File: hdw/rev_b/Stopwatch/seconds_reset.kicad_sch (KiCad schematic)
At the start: 21 parts, among them U1301 74LVC1G97, U1302 74LVC1G97, U1303 74LVC1G97, U1304 74LVC1G97, U1305 74LVC1G97, U1306 74LVC1G97, U1307 74LVC1G97

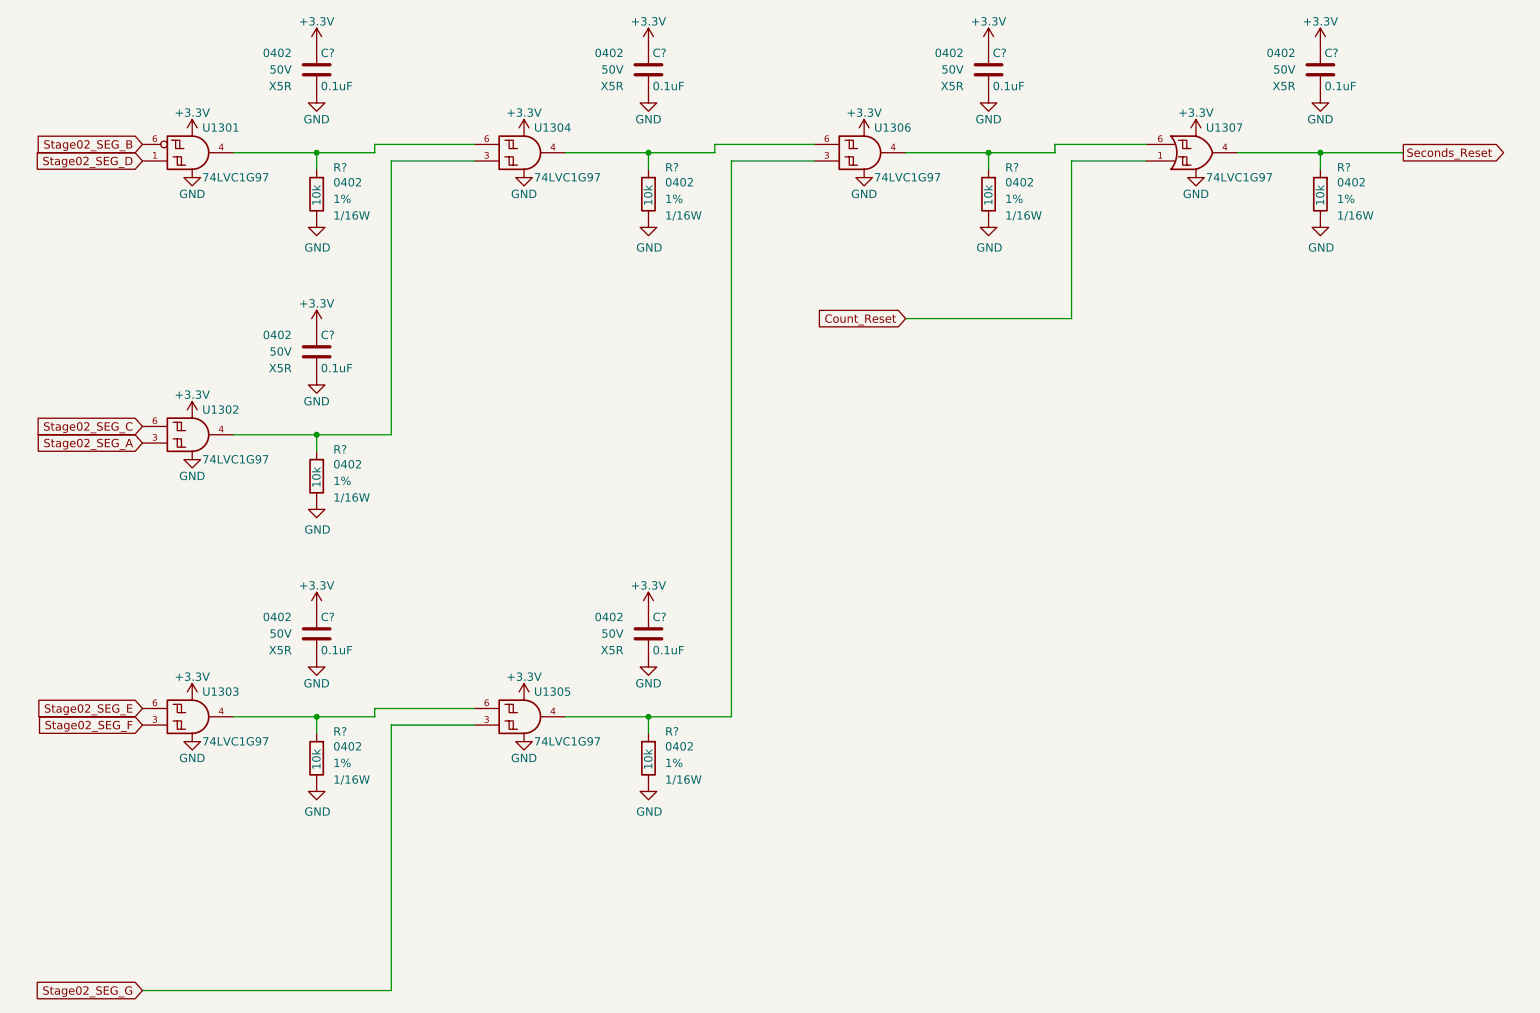
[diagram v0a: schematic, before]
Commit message: ported rev b to kicad 8
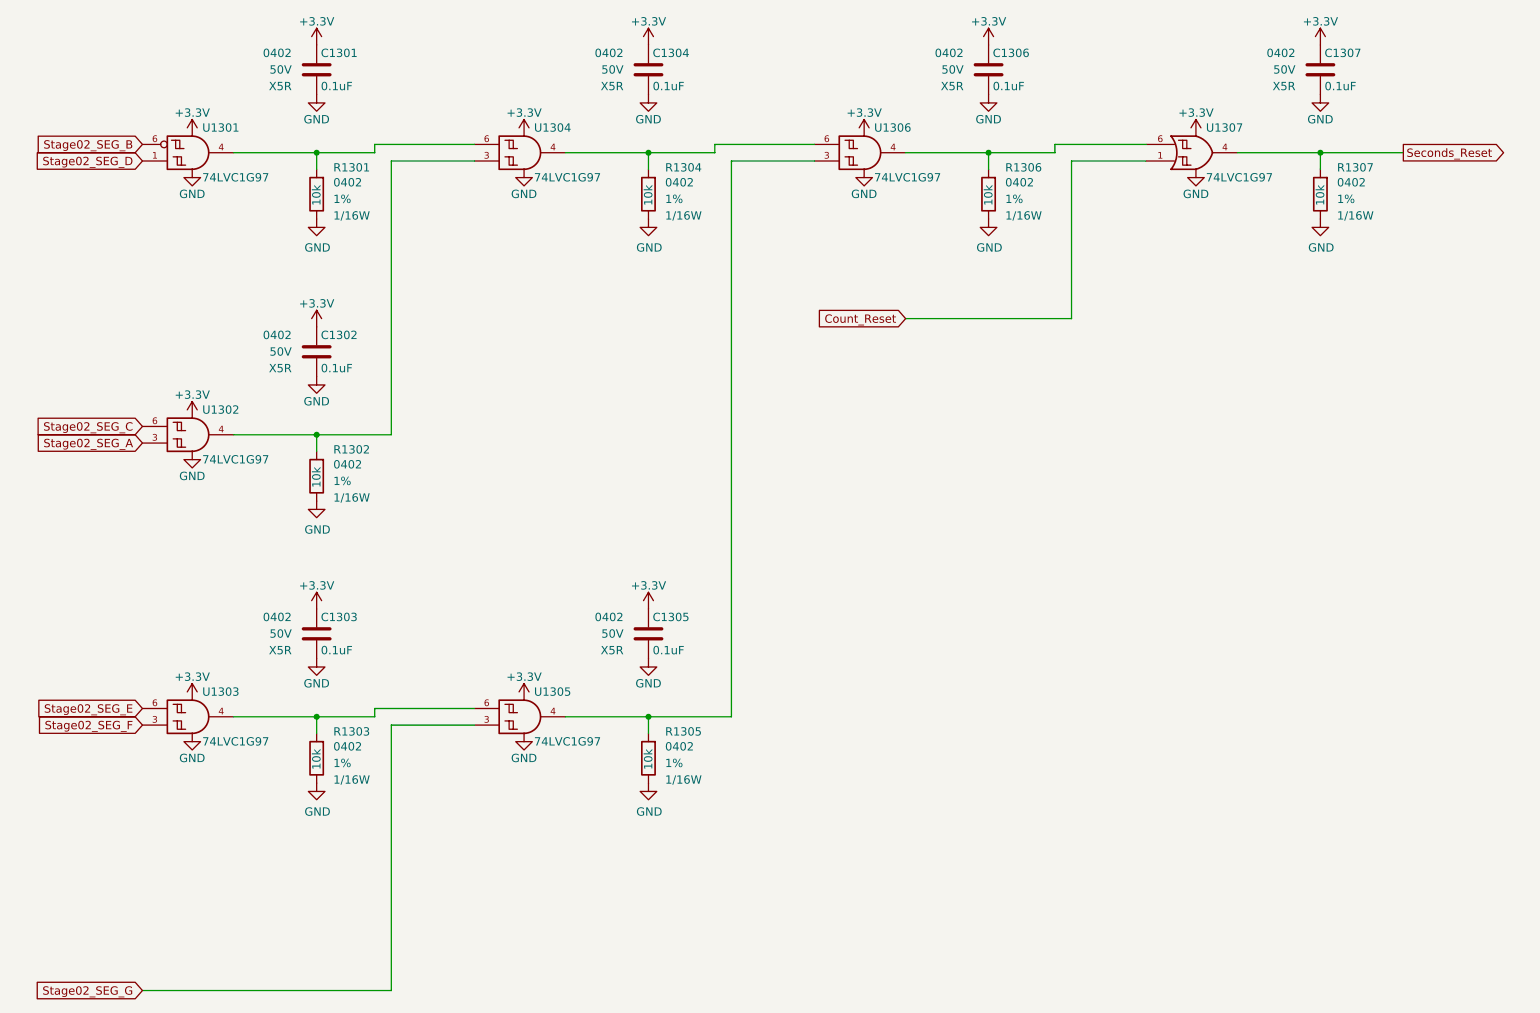
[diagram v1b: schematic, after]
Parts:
- gave numbers to parts that had none: 14

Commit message: integrated SC70 gates
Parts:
- U1301, U1302, U1303, U1304, U1305, U1306, U1307: footprint Package_SON:Fairchild_MicroPak2-6_1.0x1.0mm_P0.35mm -> Package_TO_SOT_SMD:SOT-363_SC-70-6; Digi-Key PN 296-29875-1-ND -> 296-15582-1-ND
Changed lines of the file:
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@@
 			)
 		)
-		(property "Footprint" "Package_SON:Fairchild_MicroPak2-6_1.0x1.0mm_P0.35mm"
+		(property "Footprint" "Package_TO_SOT_SMD:SOT-363_SC-70-6"
 			(at 205.74 39.37 0)
 			(effects
@@
 			)
 		)
-		(property "Digi-Key PN" "296-29875-1-ND"
+		(property "Digi-Key PN" "296-15582-1-ND"
 			(at 204.47 39.37 0)
 			(effects
@@
 			)
 		)
-		(property "Footprint" "Package_SON:Fairchild_MicroPak2-6_1.0x1.0mm_P0.35mm"
+		(property "Footprint" "Package_TO_SOT_SMD:SOT-363_SC-70-6"
 			(at 154.94 39.37 0)
 			(effects
@@
 			)
 		)
-		(property "Digi-Key PN" "296-29875-1-ND"
+		(property "Digi-Key PN" "296-15582-1-ND"
 			(at 153.67 39.37 0)
 			(effects
@@
 			)
 		)
-		(property "Footprint" "Package_SON:Fairchild_MicroPak2-6_1.0x1.0mm_P0.35mm"
+		(property "Footprint" "Package_TO_SOT_SMD:SOT-363_SC-70-6"
 			(at 52.07 82.55 0)
 			(effects
@@
 			)
 		)
-		(property "Digi-Key PN" "296-29875-1-ND"
+		(property "Digi-Key PN" "296-15582-1-ND"
 			(at 50.8 82.55 0)
 			(effects
@@
 			)
 		)
-		(property "Footprint" "Package_SON:Fairchild_MicroPak2-6_1.0x1.0mm_P0.35mm"
+		(property "Footprint" "Package_TO_SOT_SMD:SOT-363_SC-70-6"
 			(at 52.07 125.73 0)
 			(effects
@@
 			)
 		)
-		(property "Digi-Key PN" "296-29875-1-ND"
+		(property "Digi-Key PN" "296-15582-1-ND"
 			(at 50.8 125.73 0)
 			(effects
@@
 			)
 		)
-		(property "Footprint" "Package_SON:Fairchild_MicroPak2-6_1.0x1.0mm_P0.35mm"
+		(property "Footprint" "Package_TO_SOT_SMD:SOT-363_SC-70-6"
 			(at 52.07 39.37 0)
 			(effects
@@
 			)
 		)
-		(property "Digi-Key PN" "296-29875-1-ND"
+		(property "Digi-Key PN" "296-15582-1-ND"
 			(at 50.8 39.37 0)
 			(effects
@@
 			)
 		)
-		(property "Footprint" "Package_SON:Fairchild_MicroPak2-6_1.0x1.0mm_P0.35mm"
+		(property "Footprint" "Package_TO_SOT_SMD:SOT-363_SC-70-6"
 			(at 102.87 39.37 0)
 			(effects
@@
 			)
 		)
-		(property "Digi-Key PN" "296-29875-1-ND"
+		(property "Digi-Key PN" "296-15582-1-ND"
 			(at 101.6 39.37 0)
 			(effects
@@
 			)
 		)
-		(property "Footprint" "Package_SON:Fairchild_MicroPak2-6_1.0x1.0mm_P0.35mm"
+		(property "Footprint" "Package_TO_SOT_SMD:SOT-363_SC-70-6"
 			(at 102.87 125.73 0)
 			(effects
@@
 			)
 		)
-		(property "Digi-Key PN" "296-29875-1-ND"
+		(property "Digi-Key PN" "296-15582-1-ND"
 			(at 101.6 125.73 0)
 			(effects
